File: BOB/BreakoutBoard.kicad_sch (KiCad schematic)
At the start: 3 parts, among them J1 1706013, J3 1706013, J8 1706013

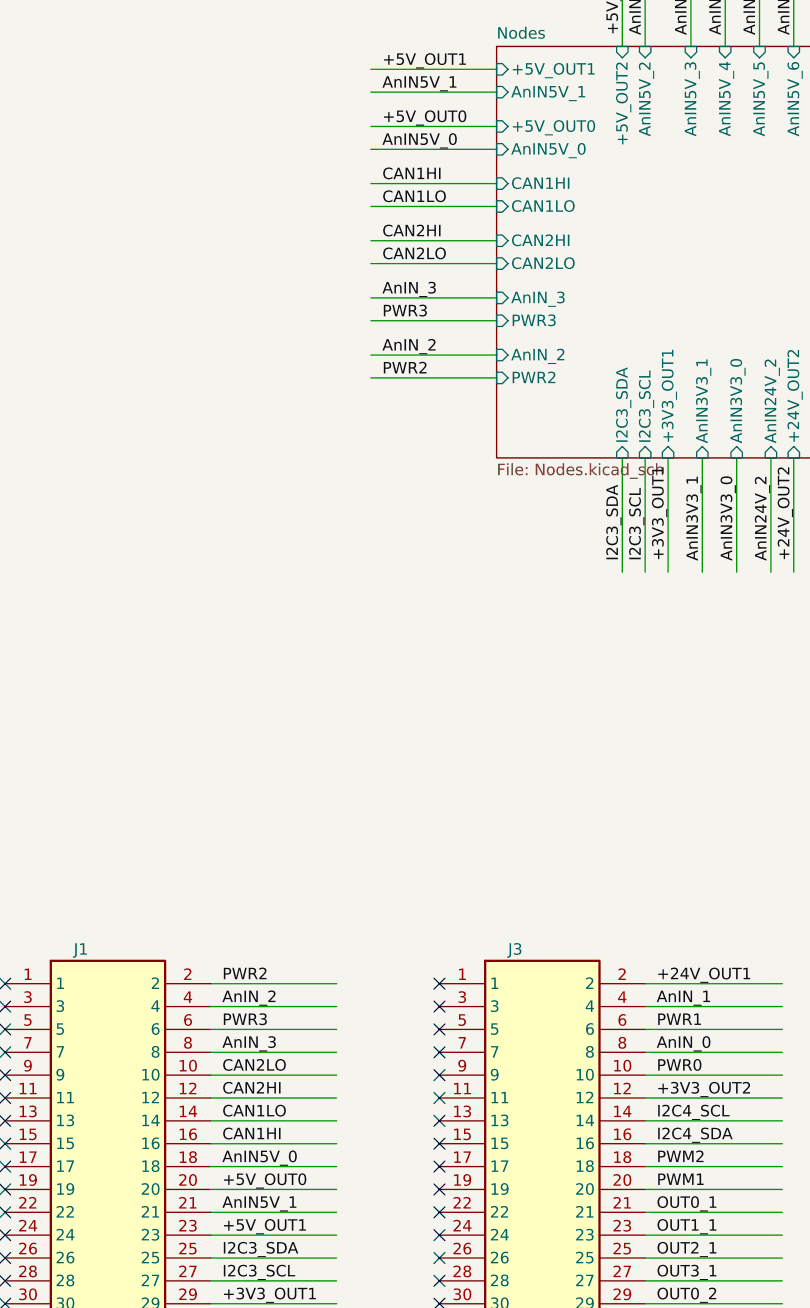
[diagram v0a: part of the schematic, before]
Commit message: BOB v2.1.2
- Reduced font size
- Fixed mistake with CAN numbers
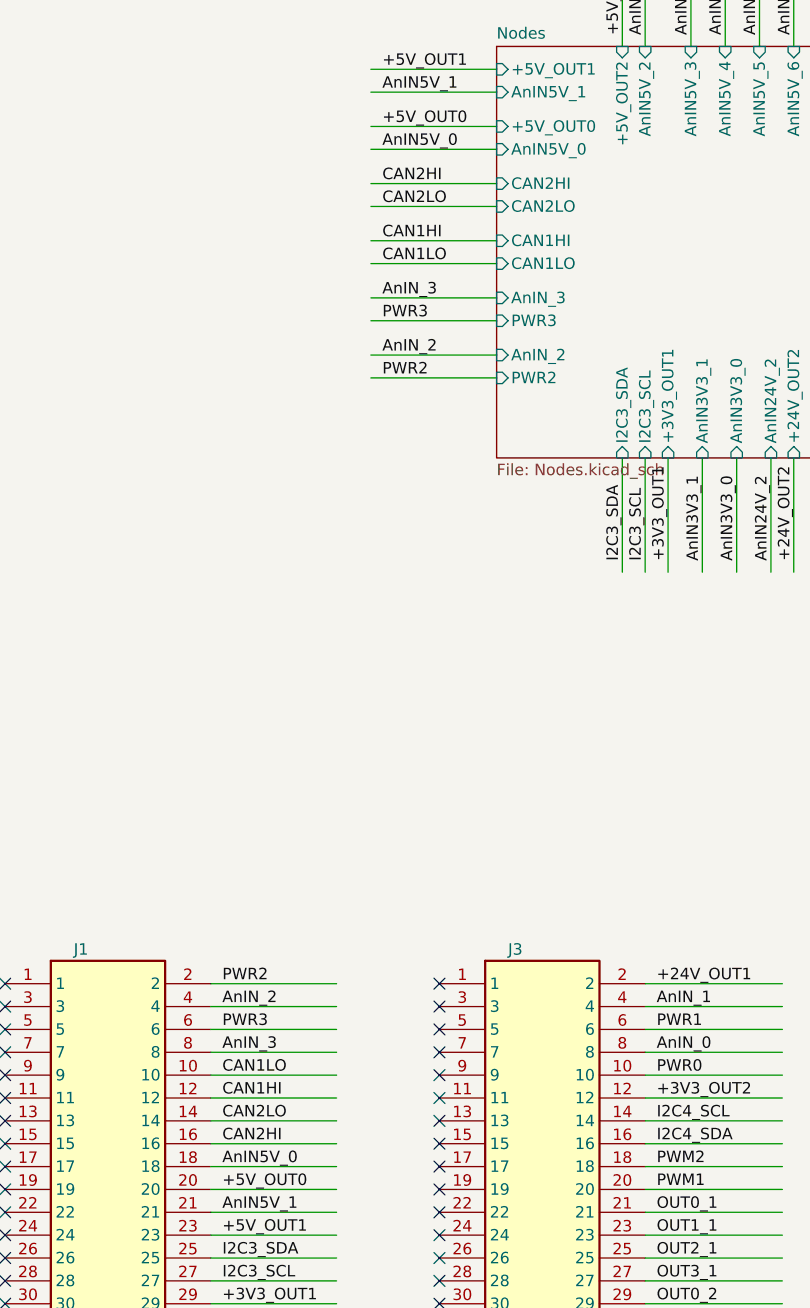
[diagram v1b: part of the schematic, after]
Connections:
- net CAN1HI: now also J1.12; no longer J1.16
- net CAN1LO: now also J1.10; no longer J1.14
- net CAN2HI: now also J1.16; no longer J1.12
- net CAN2LO: now also J1.14; no longer J1.10
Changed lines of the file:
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@@
 		)
 	)
-	(label "CAN1LO"
+	(label "CAN2LO"
 		(at 66.04 208.28 0)
 		(fields_autoplaced yes)
@@
 		)
 	)
-	(label "CAN2LO"
+	(label "CAN1LO"
 		(at 83.82 113.03 0)
 		(fields_autoplaced yes)
@@
 		)
 	)
-	(label "CAN2LO"
+	(label "CAN1LO"
 		(at 66.04 203.2 0)
 		(fields_autoplaced yes)
@@
 		)
 	)
-	(label "CAN2HI"
+	(label "CAN1HI"
 		(at 66.04 205.74 0)
 		(fields_autoplaced yes)
@@
 		)
 	)
-	(label "CAN2HI"
+	(label "CAN1HI"
 		(at 83.82 110.49 0)
 		(fields_autoplaced yes)
@@
 		)
 	)
-	(label "CAN1LO"
+	(label "CAN2LO"
 		(at 83.82 106.68 0)
 		(fields_autoplaced yes)
@@
 		)
 	)
-	(label "CAN1HI"
+	(label "CAN2HI"
 		(at 83.82 104.14 0)
 		(fields_autoplaced yes)
@@
 		)
 	)
-	(label "CAN1HI"
+	(label "CAN2HI"
 		(at 66.04 210.82 0)
 		(fields_autoplaced yes)
@@
 		)
 		(instances
-			(project "BreakoutBoard 2.0"
+			(project "BreakoutBoard"
 				(path "/87e019e3-1d3d-4a6f-8f4c-3dee61e63c51"
 					(reference "J1")
@@
 		)
 		(instances
-			(project "BreakoutBoard 2.0"
+			(project "BreakoutBoard"
 				(path "/87e019e3-1d3d-4a6f-8f4c-3dee61e63c51"
 					(reference "J8")
@@
 		)
 		(instances
-			(project "BreakoutBoard 2.0"
+			(project "BreakoutBoard"
 				(path "/87e019e3-1d3d-4a6f-8f4c-3dee61e63c51"
 					(reference "J3")
@@
 			)
 		)
+		(pin "CAN2HI" input
+			(at 96.52 104.14 180)
+			(effects
+				(font
+					(size 1.27 1.27)
+				)
+				(justify left)
+			)
+		)
 		(pin "CAN1HI" input
-			(at 96.52 104.14 180)
-			(effects
-				(font
-					(size 1.27 1.27)
-				)
-				(justify left)
-			)
-		)
-		(pin "CAN2HI" input
 			(at 96.52 110.49 180)
 			(effects
@@
 			)
 		)
+		(pin "CAN2LO" input
+			(at 96.52 106.68 180)
+			(effects
+				(font
+					(size 1.27 1.27)
+				)
+				(justify left)
+			)
+		)
 		(pin "CAN1LO" input
-			(at 96.52 106.68 180)
-			(effects
-				(font
-					(size 1.27 1.27)
-				)
-				(justify left)
-			)
-		)
-		(pin "CAN2LO" input
 			(at 96.52 113.03 180)
 			(effects
@@
 		)
 		(instances
-			(project "BreakoutBoard 2.0"
+			(project "BreakoutBoard"
 				(path "/87e019e3-1d3d-4a6f-8f4c-3dee61e63c51"
 					(page "1")
@@
 		)
 		(instances
-			(project "BreakoutBoard 2.0"
+			(project "BreakoutBoard"
 				(path "/87e019e3-1d3d-4a6f-8f4c-3dee61e63c51"
 					(page "2")
@@
 		)
 		(instances
-			(project "BreakoutBoard 2.0"
+			(project "BreakoutBoard"
 				(path "/87e019e3-1d3d-4a6f-8f4c-3dee61e63c51"
 					(page "3")
